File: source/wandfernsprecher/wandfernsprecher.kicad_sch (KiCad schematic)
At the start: 37 parts, among them J1 Hörer, J2 USB_C_Receptacle_USB2.0, Q10 AO3401A, Q11 AO3400A, SW1 Gabelschalter, SW2 Erdschalter, SW4 BOOT, U1 SIM800L, U2 ESP32-C3-WROOM-02, U5 USBLC6-2SC6

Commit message: completed layout
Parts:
- removed C18: 100n, Capacitor_SMD:C_0603_1608Metric, symbol Device:C
- removed J2: USB_C_Receptacle_USB2.0, Connector_USB:USB_C_Receptacle_HRO_TYPE-C-31-M-12, symbol Connector:USB_C_Receptacle_USB2.0
- removed R24: 10k, Resistor_SMD:R_0603_1608Metric, symbol Device:R
- removed R25, R27: 5k1, Resistor_SMD:R_0603_1608Metric, symbol Device:R
- added C19: 10µF, Capacitor_SMD:C_0603_1608Metric, symbol Device:C
- added C20: 1µF, Capacitor_SMD:C_0603_1608Metric, symbol Device:C
- added D4: 5,1V, Diode_SMD:D_SOD-123, symbol Device:D_Zener
- added J3: Conn_01x04, Connector_PinHeader_2.54mm:PinHeader_1x04_P2.54mm_Vertical, symbol Connector_Generic:Conn_01x04
- C1, C11, C16, C2, C3, C4, C5: value 100n -> 100nF
- J1, NS1, SW2: footprint FeWAp:CONN_01x04_vertical -> FeWAp:CONN_01x04_vertical_mod
- U2: footprint Espressif:ESP32-C3-WROOM-02 -> RF_Module:ESP32-C3-WROOM-02
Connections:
- net +3.3V: now also C19.2
- net +4V: now also D4.1 (K)
- net BELL_A: now also U2.4 (GPIO5/ADC2_CH0); no longer U2.6 (GPIO7)
- net BELL_B: now also U2.3 (GPIO4/ADC1_CH4); no longer U2.10 (GPIO10)
- net GND: now also C19.1, C20.1, D4.2 (A), J3.1 (Pin_1)
- net VBUS: now also J3.4 (Pin_4)
- net nsa: now also U2.10 (GPIO10); no longer U2.3 (GPIO4/ADC1_CH4)
- net nsi: now also U2.6 (GPIO7); no longer U2.4 (GPIO5/ADC2_CH0)
- net ~{RESET}: now also C20.2
- net S-: now reaches J1.4 (MIC-), U1.6 (SPK-)
- net S+: now reaches J1.3 (MIC+), U1.7 (SPK+)
- net M-: now reaches J1.2 (SPK-), U1.8 (MIC-)
- net M+: now reaches J1.1 (SPK+), U1.9 (MIC+)
- net plug_D+ renamed plug.D+
- net plug.D+: now also J3.2 (Pin_2)
- net plug_D- renamed plug.D-
- net plug.D-: now also J3.3 (Pin_3)
- no-connect marks 8 -> 9
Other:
- sheet Power Supply ports: added +3.3V, +BATT, 4.0V, VBUS; removed none
- note added: "NEXT VERSION: add USB-C connection"
- note added: "TODO: - USB connector for in-case charging and programming"
- note removed: "TODO: - charger - bell voltage booster - bell H-bridge"
- moved on the sheet: C11, C17, C5, R19, R5, R6, R7

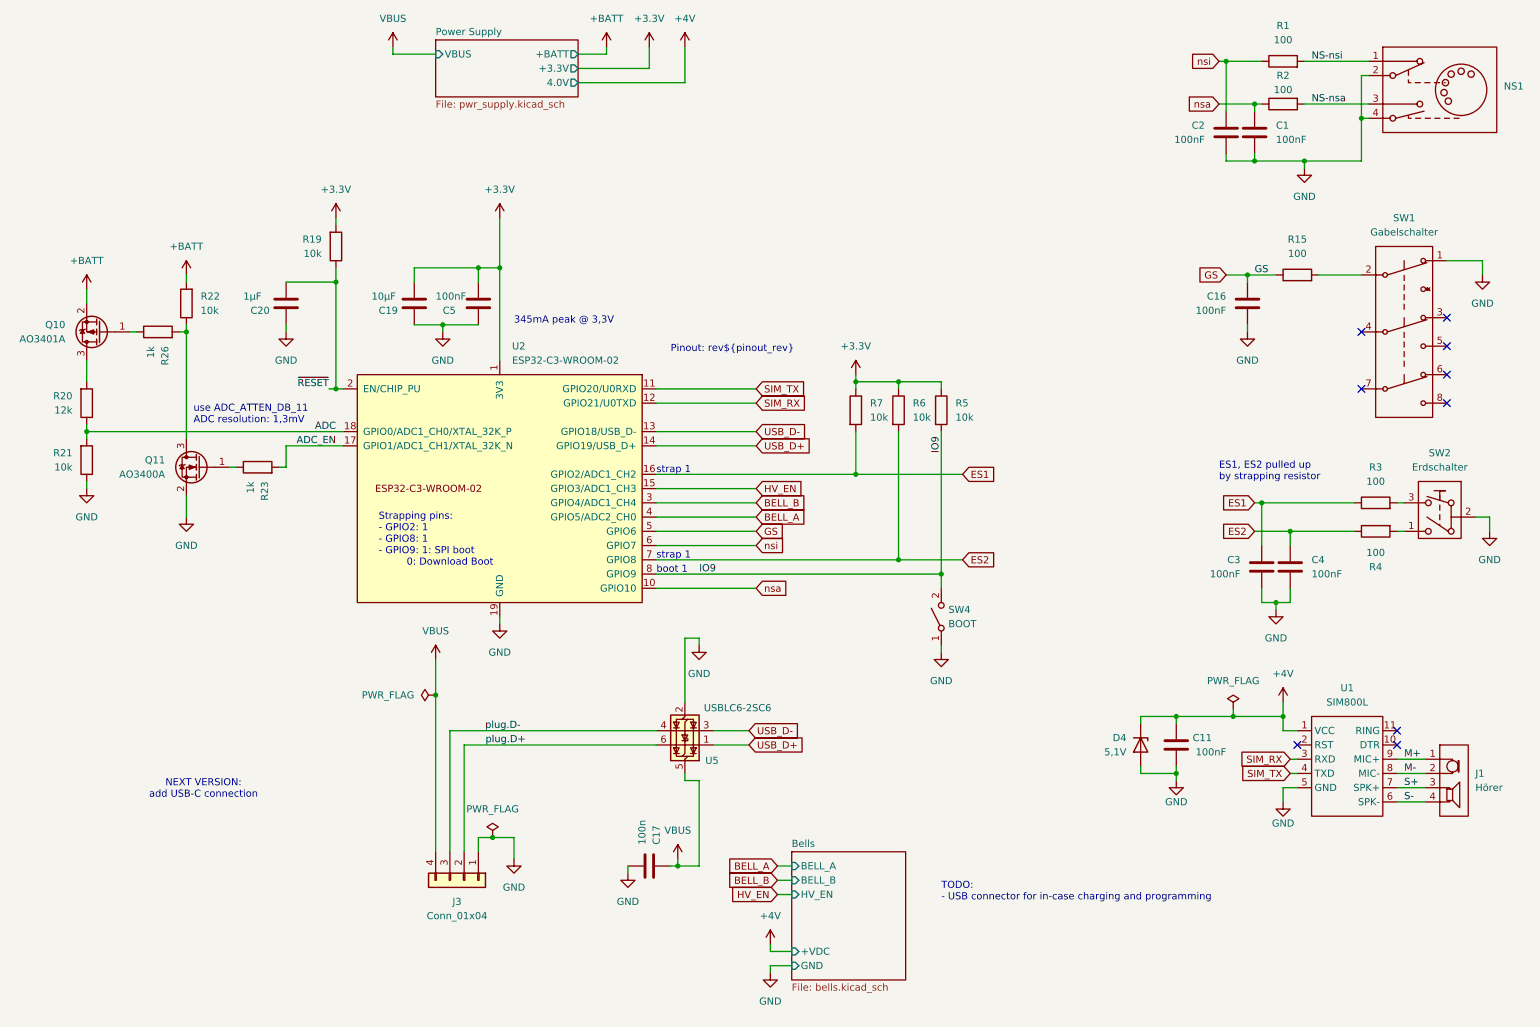
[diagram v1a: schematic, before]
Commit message: added ibom added switch holder FreeCAD file added Vin header and ideal diodes, finalized layout
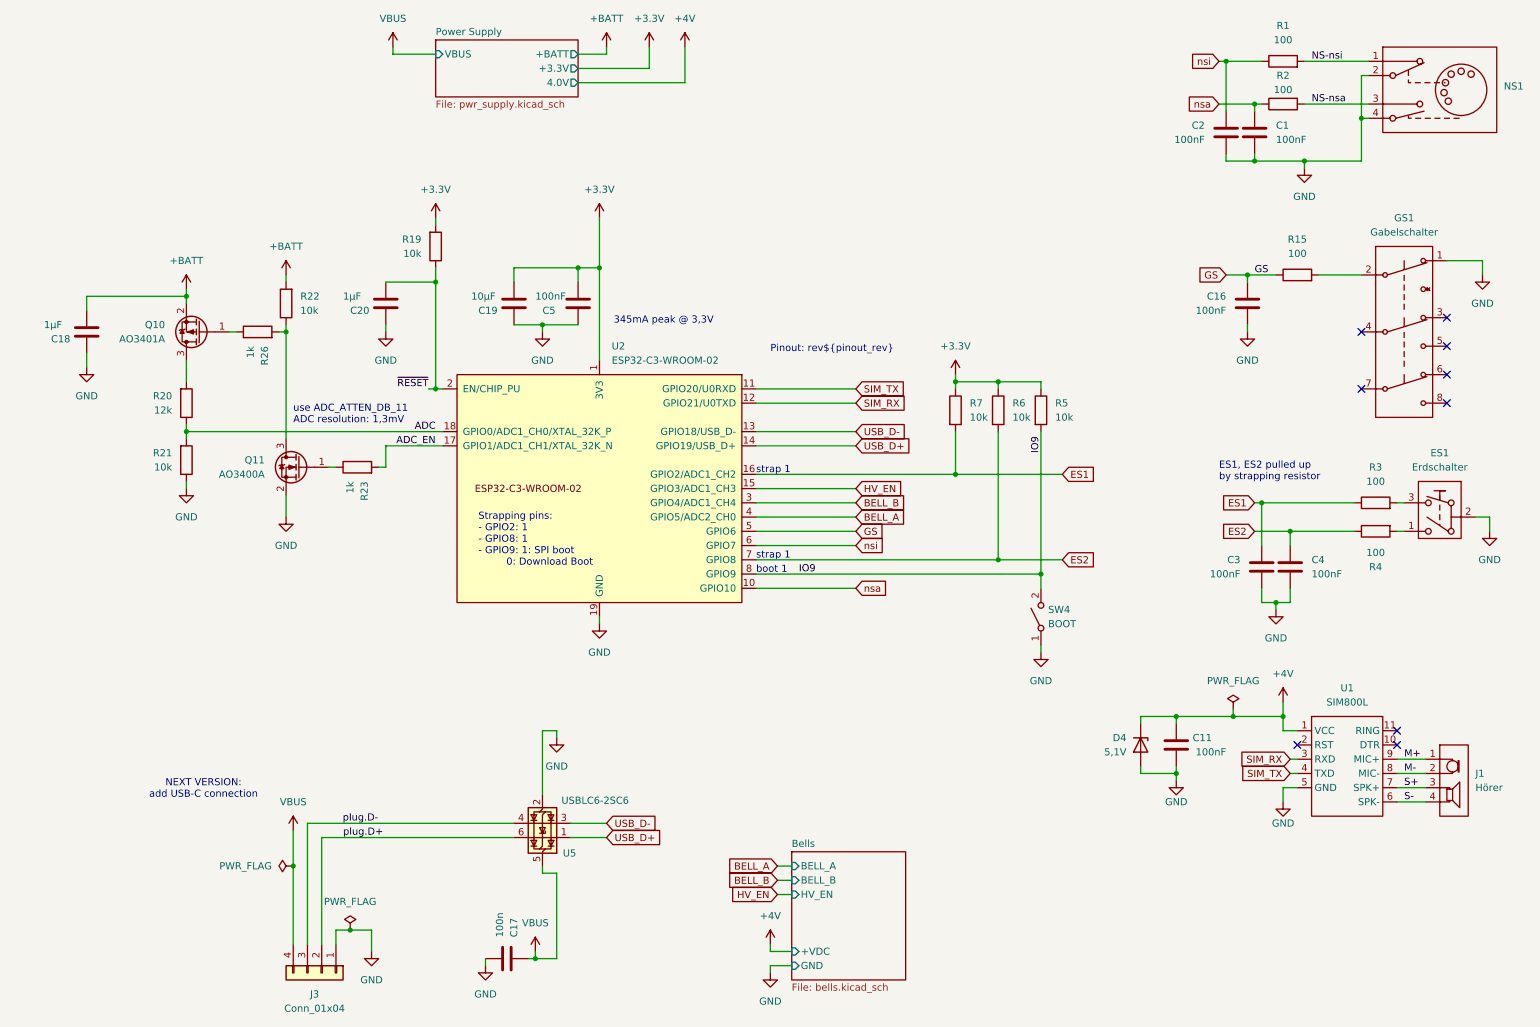
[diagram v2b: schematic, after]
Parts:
- added C18: 1µF, Capacitor_SMD:C_0603_1608Metric, symbol Device:C
- renumbered SW2 to ES1, SW1 to GS1
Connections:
- net +BATT: now also C18.2
- net GND: now also C18.1
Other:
- note removed: "TODO: - USB connector for in-case charging and programming"
- moved on the sheet: C17, C19, C20, C5, J3, Q10, Q11, R19, R20, R21, R22, R23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

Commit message: cleanup and 3D-Models fixed submodule updated README
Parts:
- D4: value 5,1V -> 5.1V
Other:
- note added: "345mA peak @ 3.3V"
- note added: "use ADC_ATTEN_DB_11 ADC resolution: 1.3mV"
- note removed: "345mA peak @ 3,3V"
- note removed: "use ADC_ATTEN_DB_11 ADC resolution: 1,3mV"
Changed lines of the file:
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@@
 	(title_block
 		(title "${title}")
+		(date "01.11.2024")
 		(rev "${revision}")
 		(company "author: ${author}")
@@
 		)
 	)
-	(text "345mA peak @ 3,3V"
+	(text "345mA peak @ 3.3V"
 		(exclude_from_sim no)
 		(at 120.65 73.66 0)
@@
 		)
 	)
-	(text "use ADC_ATTEN_DB_11\nADC resolution: 1,3mV"
+	(text "use ADC_ATTEN_DB_11\nADC resolution: 1.3mV"
 		(exclude_from_sim no)
 		(at 63.5 91.44 0)
@@
 	(label "ADC_EN"
 		(at 88.9 95.25 180)
-		(fields_autoplaced yes)
 		(effects
 			(font
@@
 	(label "M+"
 		(at 261.62 151.13 0)
-		(fields_autoplaced yes)
 		(effects
 			(font
@@
 	(label "plug.D-"
 		(at 72.3251 162.56 0)
-		(fields_autoplaced yes)
 		(effects
 			(font
@@
 	(label "IO9"
 		(at 153.67 118.11 0)
-		(fields_autoplaced yes)
 		(effects
 			(font
@@
 	(label "~{RESET}"
 		(at 87.63 85.09 180)
-		(fields_autoplaced yes)
 		(effects
 			(font
@@
 	(label "IO9"
 		(at 196.85 96.52 90)
-		(fields_autoplaced yes)
 		(effects
 			(font
@@
 	(label "S+"
 		(at 261.62 156.21 0)
-		(fields_autoplaced yes)
 		(effects
 			(font
@@
 	(label "NS-nsa"
 		(at 245.11 34.29 0)
-		(fields_autoplaced yes)
 		(effects
 			(font
@@
 	(label "S-"
 		(at 261.62 158.75 0)
-		(fields_autoplaced yes)
 		(effects
 			(font
@@
 	(label "M-"
 		(at 261.62 153.67 0)
-		(fields_autoplaced yes)
 		(effects
 			(font
@@
 	(label "NS-nsi"
 		(at 245.11 26.67 0)
-		(fields_autoplaced yes)
 		(effects
 			(font
@@
 	(label "plug.D+"
 		(at 72.39 165.1 0)
-		(fields_autoplaced yes)
 		(effects
 			(font
@@
 	(label "ADC"
 		(at 88.9 92.71 180)
-		(fields_autoplaced yes)
 		(effects
 			(font
@@
 	(label "GS"
 		(at 234.95 64.77 0)
-		(fields_autoplaced yes)
 		(effects
 			(font
@@
 			)
 		)
-		(property "Value" "5,1V"
+		(property "Value" "5.1V"
 			(at 212.09 149.8599 90)
 			(effects
